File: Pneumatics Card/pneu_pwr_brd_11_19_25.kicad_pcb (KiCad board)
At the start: 4 copper layers, 62 x 62 mm, 74 parts, among them J1 2X1, J10 Conn_01x02, J11 Conn_01x02, J12 2X1, J2 2X1, J3 2X1, J4 2X1, J5 2X1, J6 2X1, J7 Conn_01x03_Pin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

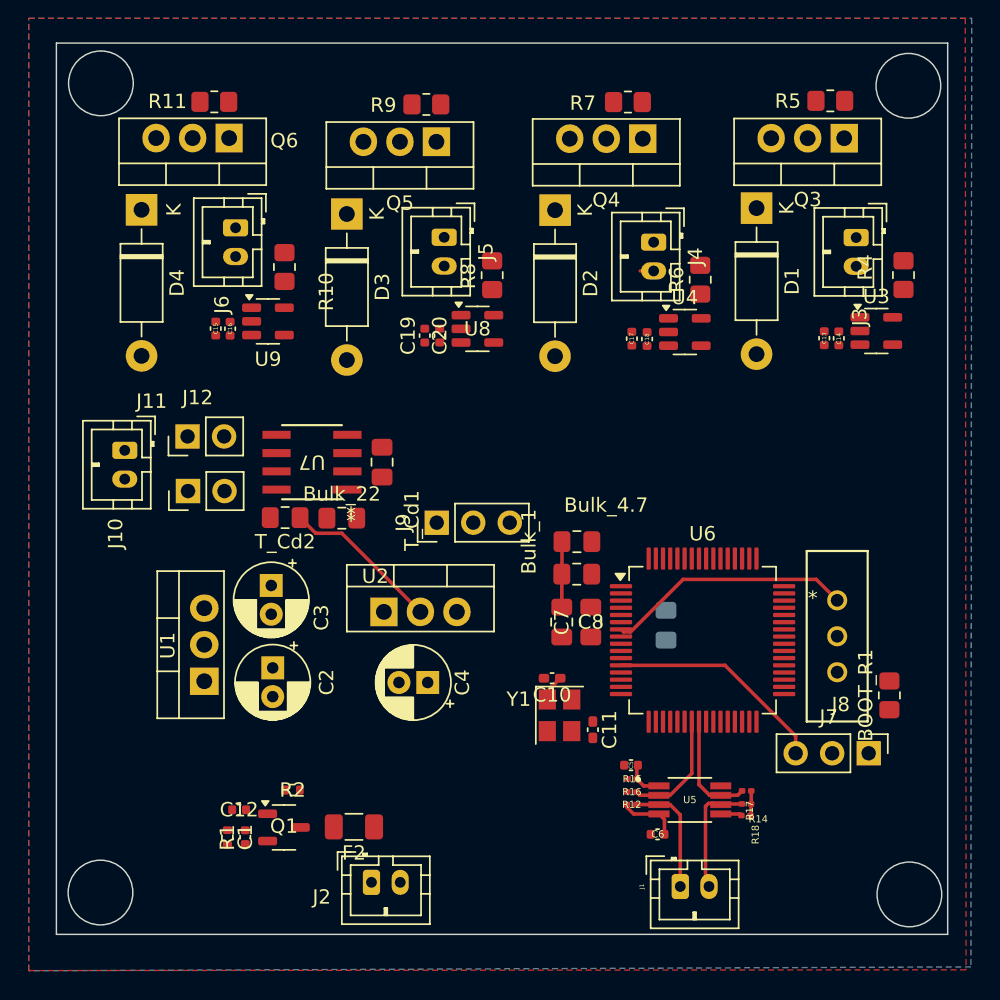
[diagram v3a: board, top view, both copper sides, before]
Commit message: Fixed the footprints and silkscreens
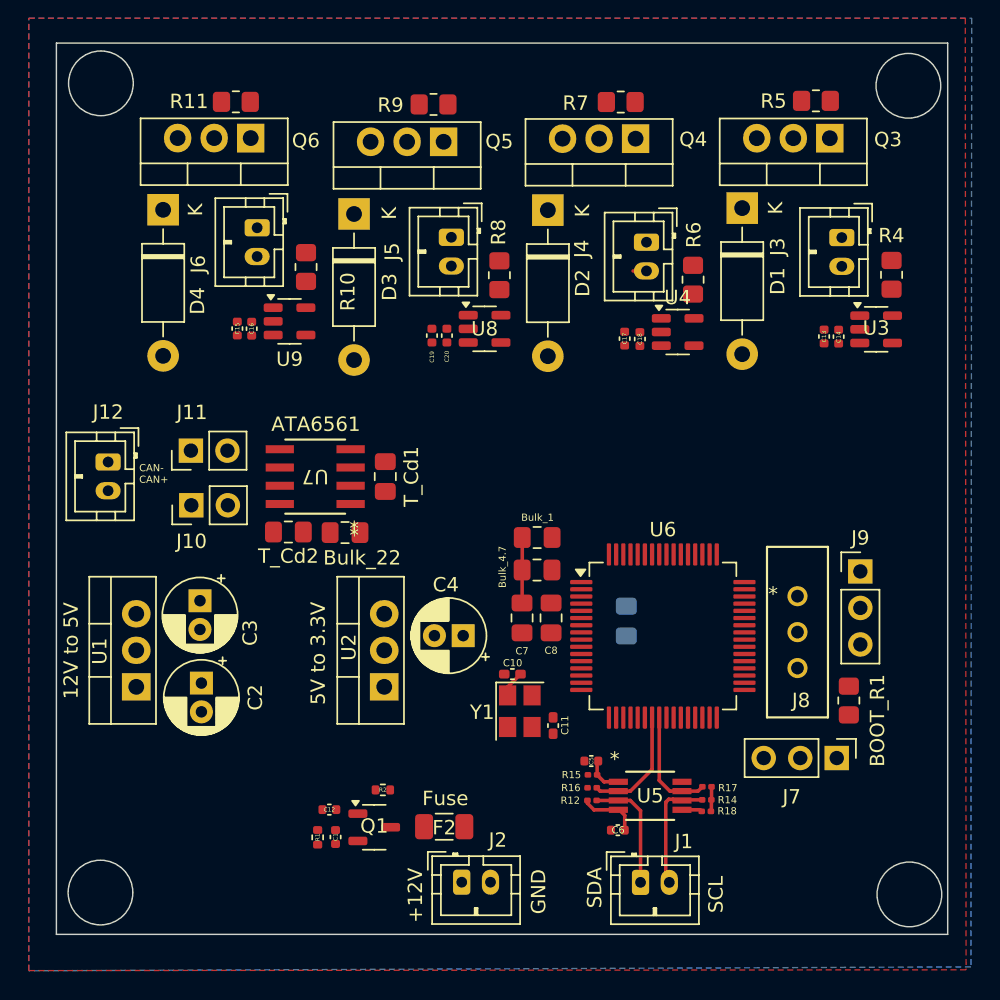
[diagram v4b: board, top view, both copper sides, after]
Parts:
- U5: footprint TCA4307:SOP65P490X110-8N -> custom_components:SOIC8_DGK_TEX
- moved J9 29.7 mm to (134.0, 54.8), turned to 0 degrees
- moved C1 6.28 mm to (97.5, 73.3)
- moved C12 6.28 mm to (97.1, 71.4)
- moved J2 6.28 mm to (106.3, 76.4)
- moved Q1 6.28 mm to (100.2, 72.6)
- moved R1 6.28 mm to (96.3, 73.3)
- moved R2 6.28 mm to (100.8, 70.0)
- moved F2 6.28 mm to (105.1, 72.6)
- moved U2 5.22 mm to (100.9, 62.8), turned to 90 degrees
- moved C3 5.07 mm to (88.1, 56.8)
- moved C2 5.07 mm to (88.2, 62.6)
- moved U1 4.75 mm to (83.7, 62.8)
- moved C4 4.09 mm to (106.4, 59.3)
- moved BOOT_R1 2.84 mm to (133.2, 63.8)
- moved J8 2.78 mm to (129.6, 56.5)
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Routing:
- net 3.3V: track 39.2 -> 10.9 mm
- net /NRST: track 15.4 -> 0.00 mm
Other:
- board text added: "+12V"
- board text added: "12V to 5V"
- board text added: "5V to 3.3V"
- board text added: "ATA6561"
- board text added: "CAN- CAN+"
- board text added: "Fuse"
- board text added: "GND"
- board text added: "SCL"
- board text added: "SDA"

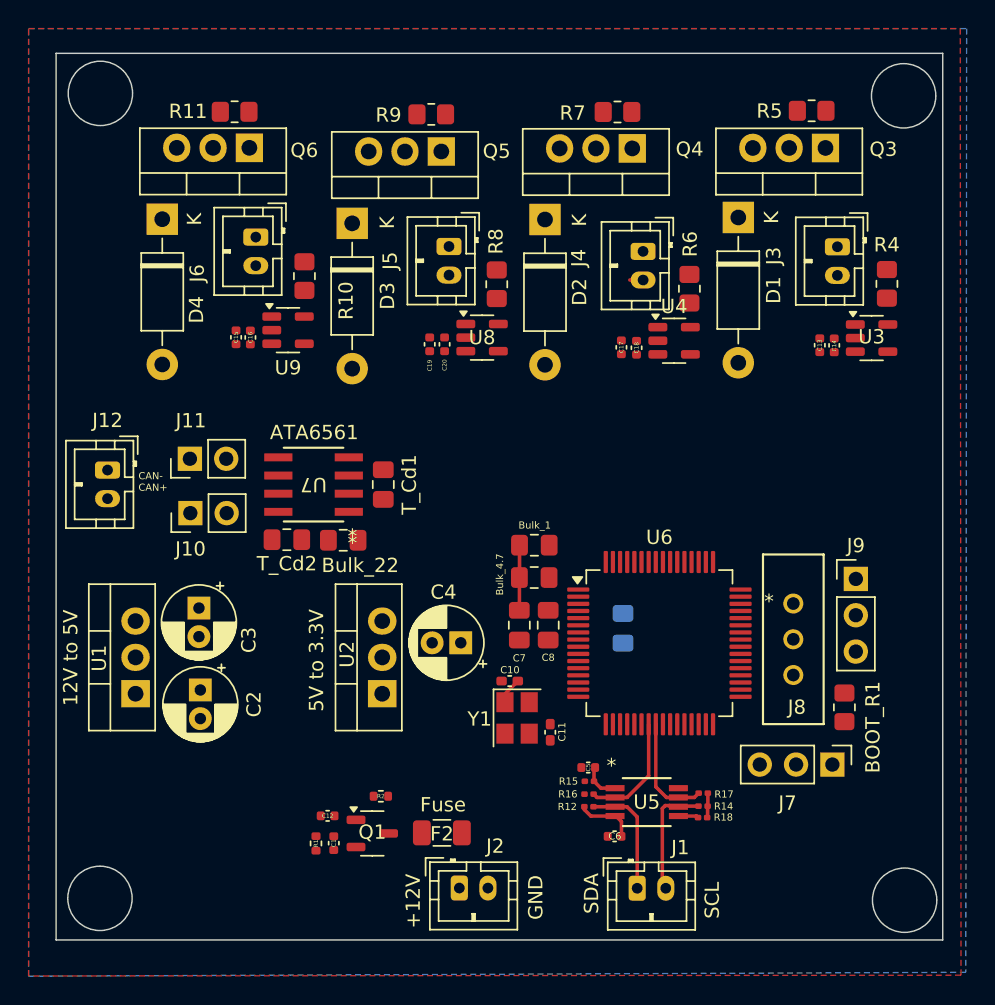
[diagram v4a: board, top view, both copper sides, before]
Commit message: Made most of routing
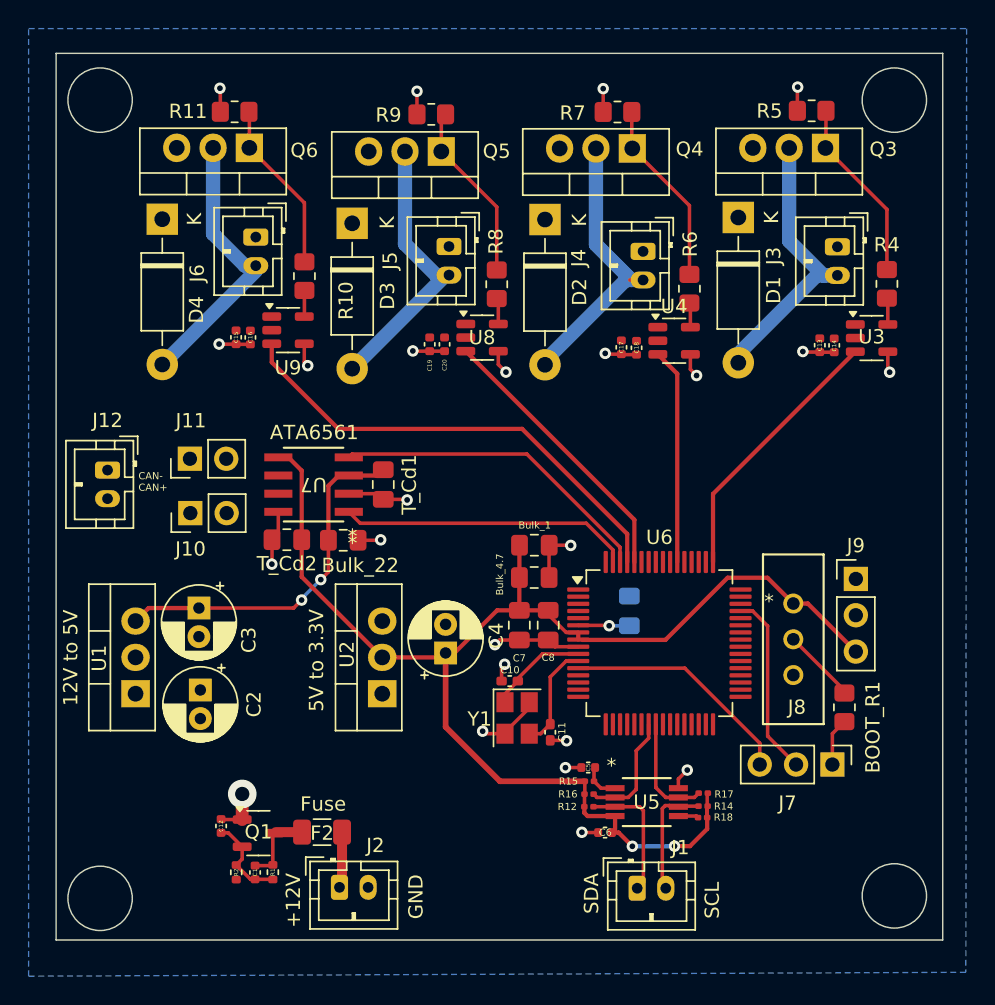
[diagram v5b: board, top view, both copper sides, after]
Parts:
- moved R2 11.4 mm to (90.7, 75.3), turned to 90 degrees
- moved J2 8.38 mm to (97.9, 76.4)
- moved F2 8.38 mm to (96.7, 72.5)
- moved Q1 7.96 mm to (92.2, 72.6)
- moved C12 7.48 mm to (89.6, 72.1), turned to 90 degrees
- moved C1 5.87 mm to (92.0, 75.3), turned to 90 degrees
- moved R1 3.63 mm to (93.2, 75.3), turned to 90 degrees
- moved C9 1.29 mm to (118.2, 57.0), turned to -90 degrees
- moved C4 1.28 mm to (105.3, 60.0), turned to 90 degrees
- moved C6 0.72 mm to (116.5, 72.5)
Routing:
- net 3.3V: track 10.9 -> 94.6 mm, vias 0 -> 2
- net GND: track 0.00 -> 52.3 mm, vias 0 -> 23
- net S4CTRL: track 0.00 -> 33.1 mm
- net 5V: track 0.00 -> 25.3 mm, vias 0 -> 2
- net FDCAN_RX: track 0.00 -> 22.8 mm
- net SLN1-: track 0.00 -> 20.7 mm
- net SLN2-: track 0.93 -> 21.5 mm
- net FDCAN_TX: track 0.00 -> 20.4 mm
- net SLN3-: track 0.00 -> 19.9 mm
- net S3CTRL: track 0.00 -> 19.6 mm
- net SLN4-: track 0.37 -> 19.9 mm
- net S1CTRL: track 0.00 -> 18.8 mm
- net /NRST: track 0.00 -> 16.4 mm
- net S2CTRL: track 0.00 -> 15.1 mm
- net Net-(Q4-G): track 0.00 -> 13.0 mm
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- removed copper zone on F.Cu, net GND
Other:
- outline, holes or cut-outs redrawn

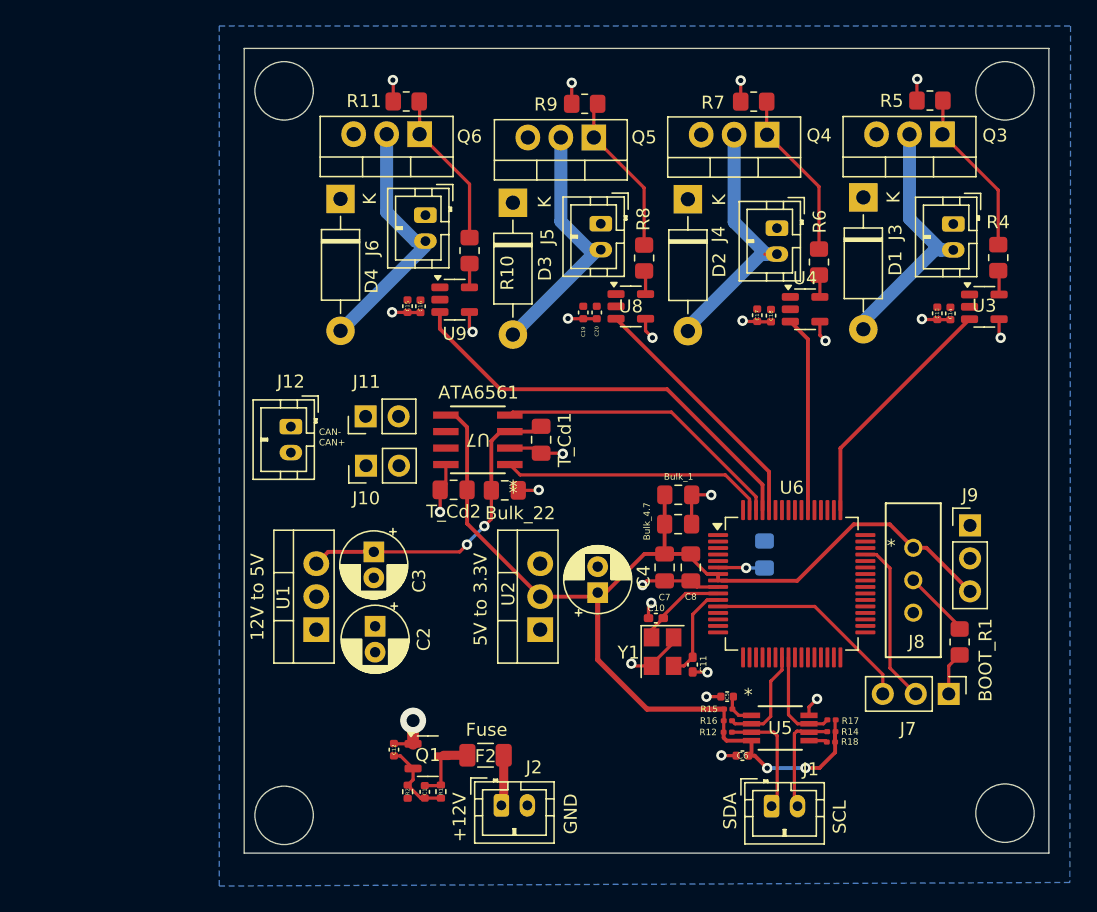
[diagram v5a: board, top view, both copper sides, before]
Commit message: Finished Tracing
Added USART, Mounting Hole, Stiching Vias, Proper 12V connection.
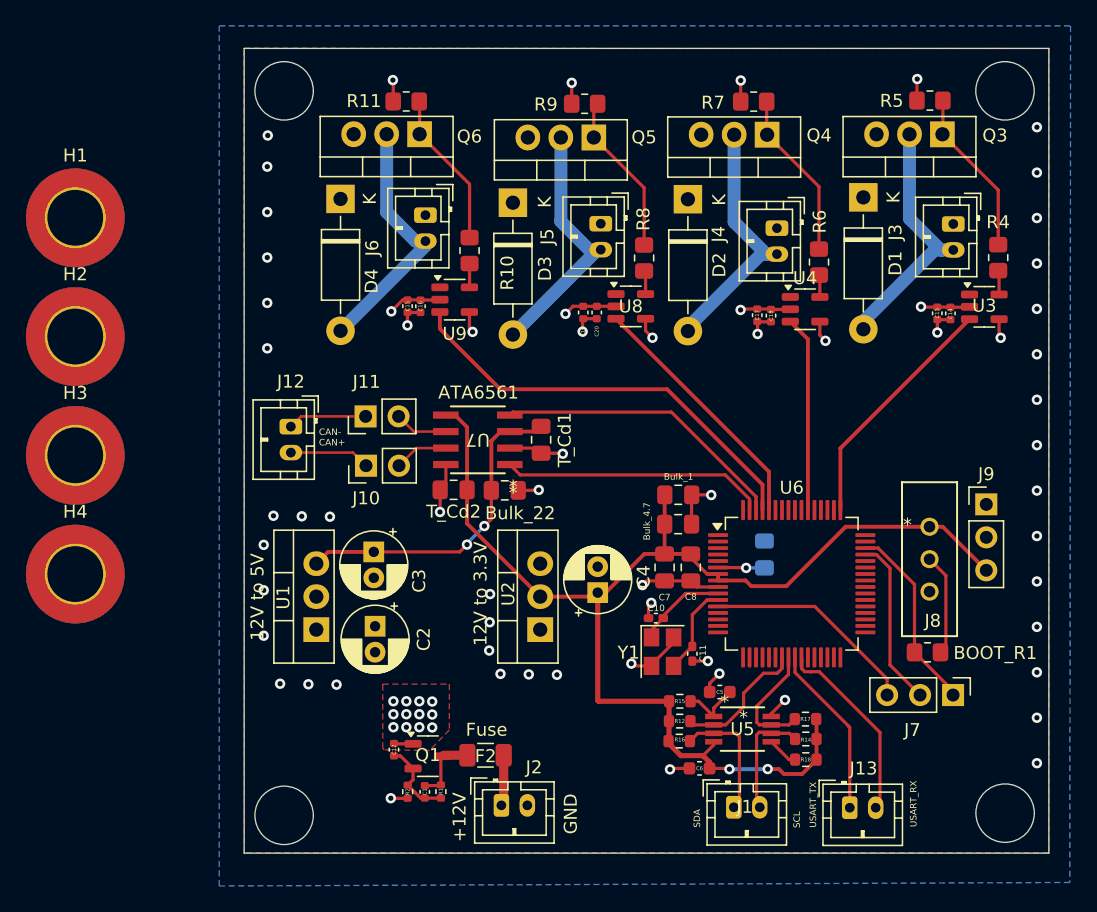
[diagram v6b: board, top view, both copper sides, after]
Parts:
- added H1: MountingHole, MountingHole:MountingHole_4.3mm_M4_ISO7380_Pad_TopBottom, F.Cu at (65.1, 31.1)
- added H2: MountingHole, MountingHole:MountingHole_4.3mm_M4_ISO7380_Pad_TopBottom, F.Cu at (65.1, 40.2)
- added H3: MountingHole, MountingHole:MountingHole_4.3mm_M4_ISO7380_Pad_TopBottom, F.Cu at (65.1, 49.4)
- added H4: MountingHole, MountingHole:MountingHole_4.3mm_M4_ISO7380_Pad_TopBottom, F.Cu at (65.1, 58.5)
- added J13: 2X1, Connector_JST:JST_PH_B2B-PH-K_1x02_P2.00mm_Vertical, F.Cu at (124.8, 76.5)
- C5, C6: footprint Capacitor_SMD:C_0402_1005Metric -> Capacitor_SMD:C_0603_1608Metric
- R12, R14, R15, R16, R17, R18: footprint Capacitor_SMD:C_0201_0603Metric -> Resistor_SMD:R_0603_1608Metric
- moved R12 3.80 mm to (111.6, 71.4)
- moved R15 3.78 mm to (111.7, 68.3)
- moved R16 3.71 mm to (111.7, 69.9)
- moved C6 3.45 mm to (113.2, 73.5)
- moved J1 2.91 mm to (115.8, 76.5)
- moved U5 2.91 mm to (116.5, 70.5)
- moved BOOT_R1 2.60 mm to (130.7, 64.6), turned to 0 degrees
- moved R18 2.36 mm to (121.4, 72.8)
- moved J8 2.05 mm to (130.9, 54.9)
- moved J9 2.05 mm to (135.3, 53.2)
- moved R14 2.05 mm to (121.4, 71.3)
- moved R17 2.01 mm to (121.3, 69.7)
- moved C11 0.84 mm to (112.6, 64.7)
- moved C5 0.67 mm to (114.7, 67.6)
- moved J7 0.34 mm to (132.7, 67.9)
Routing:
- net (no net): track 0.00 -> 28.2 mm
- net 12V: track 3.28 -> 17.4 mm, vias 1 -> 16
- net /SWCLK: track 3.35 -> 14.7 mm
- net CAN+: track 0.00 -> 10.4 mm
- net CAN-: track 0.00 -> 10.2 mm
- net 3.3V: track 94.6 -> 97.4 mm
- net Net-(J8-Pin_2): track 5.24 -> 7.88 mm
- net SDA: track 8.28 -> 10.4 mm
- net Net-(U5-EN): track 2.73 -> 4.66 mm
- net GND: track 52.3 -> 54.1 mm, vias 23 -> 60
- net SCL: track 7.89 -> 9.23 mm
- net SLN2-: track 21.5 -> 20.5 mm
- net Net-(U5-READY): track 1.48 -> 2.41 mm
- net SDA_ext: track 9.21 -> 9.72 mm
- added copper zone on F.Cu, net 12V
- added copper zone on F.Cu, net GND
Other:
- board text added: "12V to 3.3V"
- board text added: "USART_RX"
- board text added: "USART_TX"
- board text removed: "5V to 3.3V"

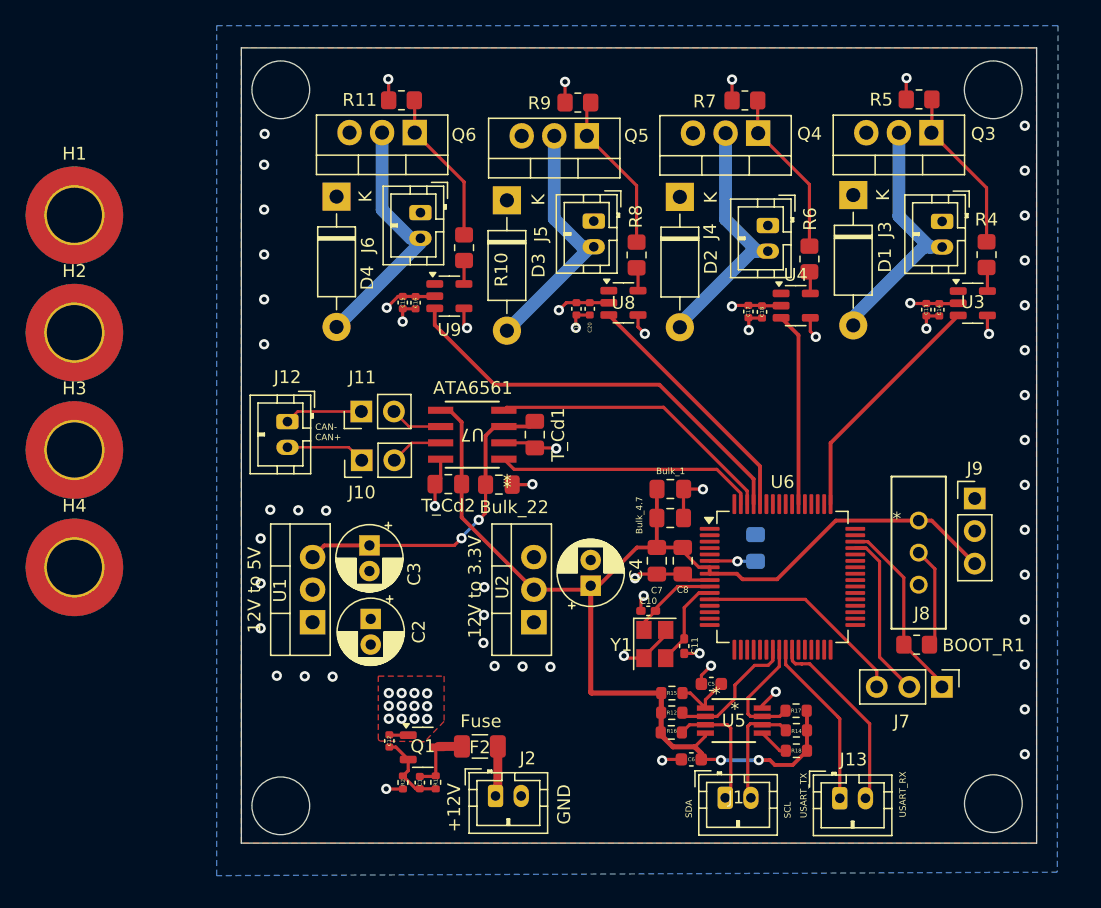
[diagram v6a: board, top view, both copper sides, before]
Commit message: Integrated Mounting Holes and made PCB 65x65
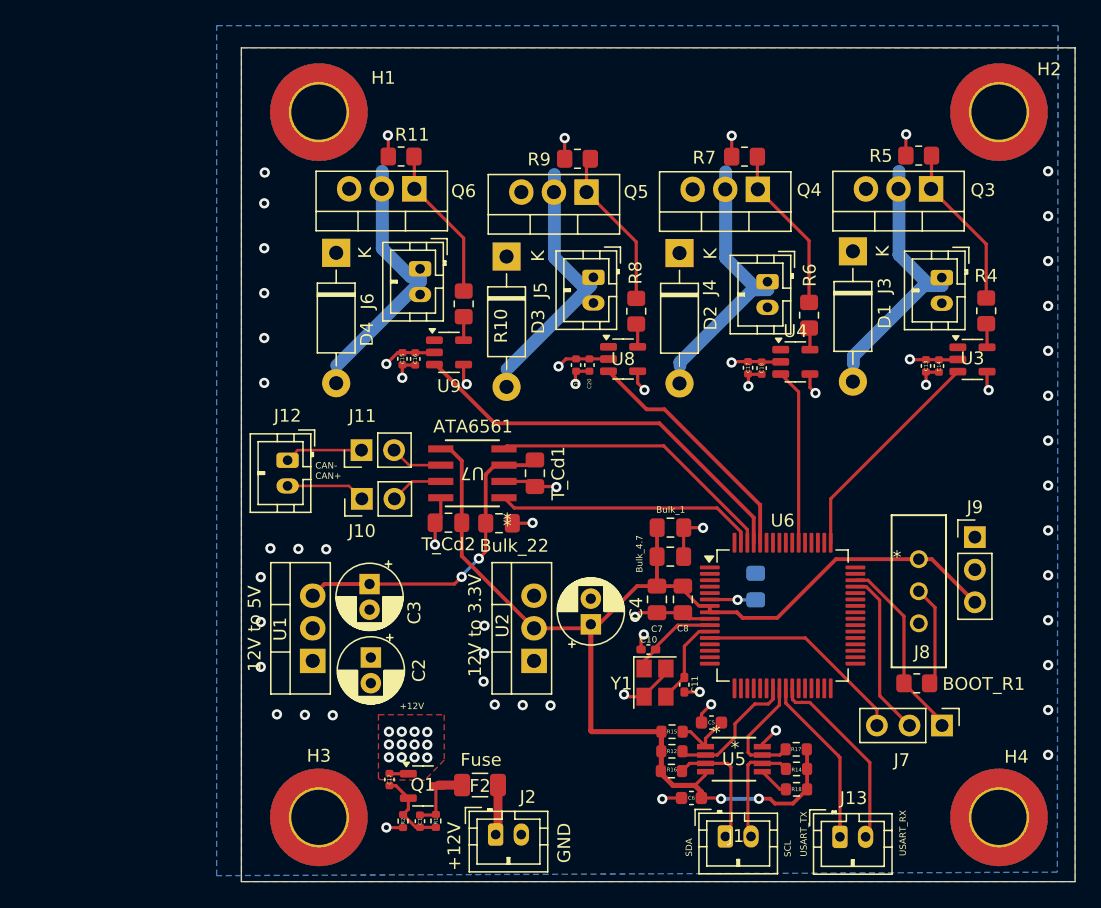
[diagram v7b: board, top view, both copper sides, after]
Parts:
- moved H4 74.7 mm to (137.2, 78.0)
- moved H2 74.1 mm to (137.2, 23.1)
- moved H3 34.4 mm to (84.1, 78.0)
- moved H1 20.7 mm to (84.1, 23.1)
- moved C13 4.38 mm to (131.5, 42.8)
- moved C14 4.38 mm to (132.5, 42.9)
- moved C15 4.38 mm to (90.7, 42.3)
- moved C16 4.38 mm to (91.7, 42.3)
- moved C17 4.38 mm to (117.6, 43.0)
- moved C18 4.38 mm to (118.7, 43.0)
- moved C19 4.38 mm to (104.2, 42.8)
- moved C20 4.38 mm to (105.2, 42.8)
- moved D2 4.38 mm to (112.3, 34.1)
- moved D3 4.38 mm to (98.8, 34.3)
- moved D4 4.38 mm to (85.5, 34.0)
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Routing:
- net S1CTRL: track 18.8 -> 17.4 mm
- net S2CTRL: track 15.1 -> 13.7 mm
- net S4CTRL: track 33.1 -> 31.8 mm
- net S3CTRL: track 19.6 -> 19.1 mm
- net GND: vias 60 -> 59
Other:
- board size 62 x 62 mm -> 65 x 65 mm
